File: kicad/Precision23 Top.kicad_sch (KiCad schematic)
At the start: 18 parts, among them J503 Conn_02x03_Odd_Even, J505 Conn_01x06, J506 Conn_01x06, J596 STANDOFF, J597 STANDOFF, J598 STANDOFF, J599 STANDOFF, U501 SAM-M10Q, U502 741G157, U503 741G157, U504 741G157

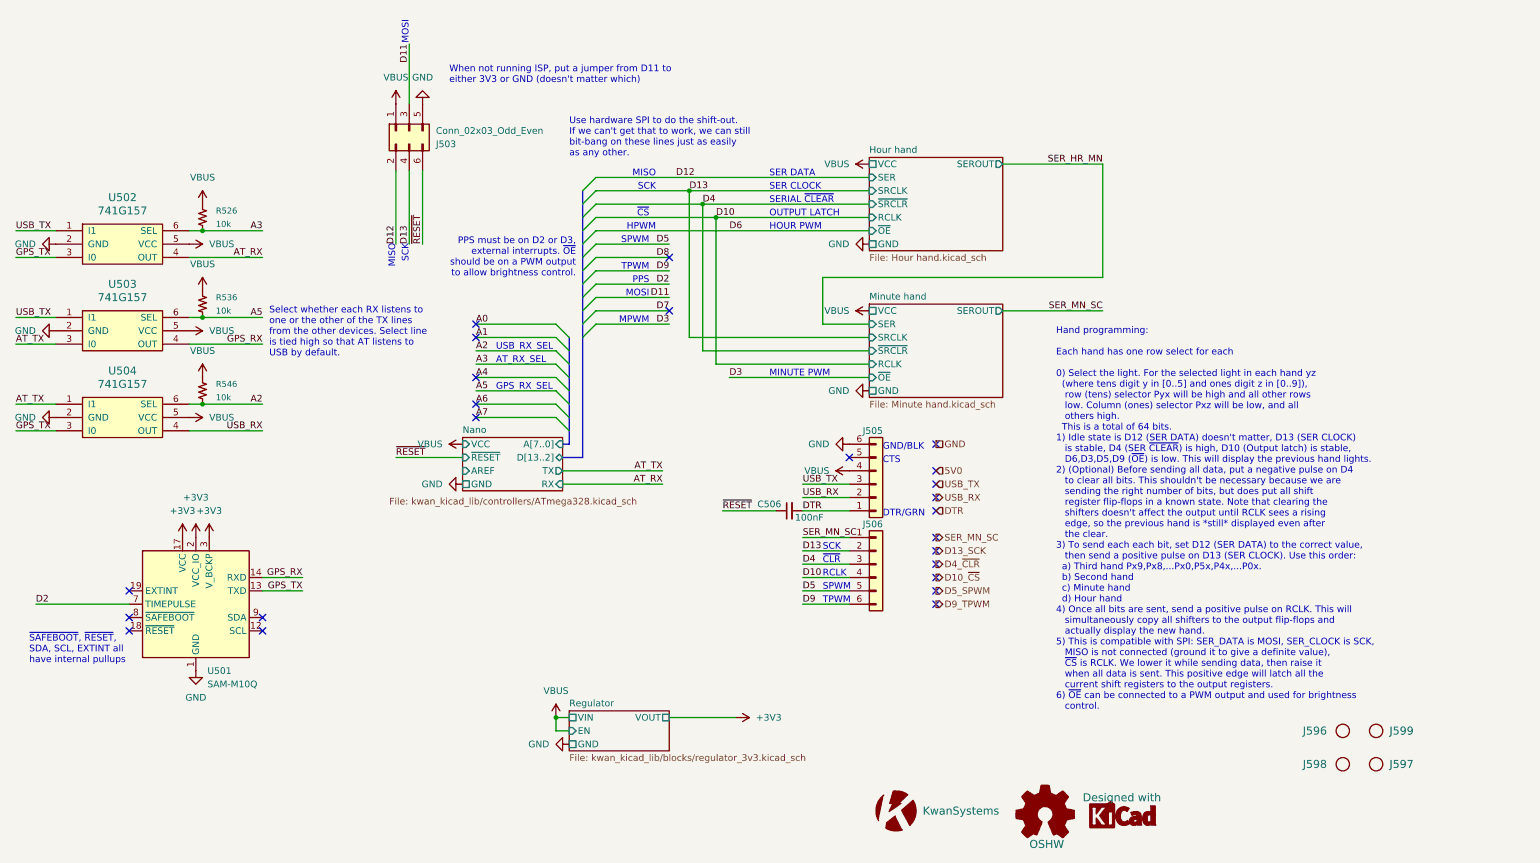
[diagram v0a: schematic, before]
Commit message: Added top and bottom schematics to support refactor of board
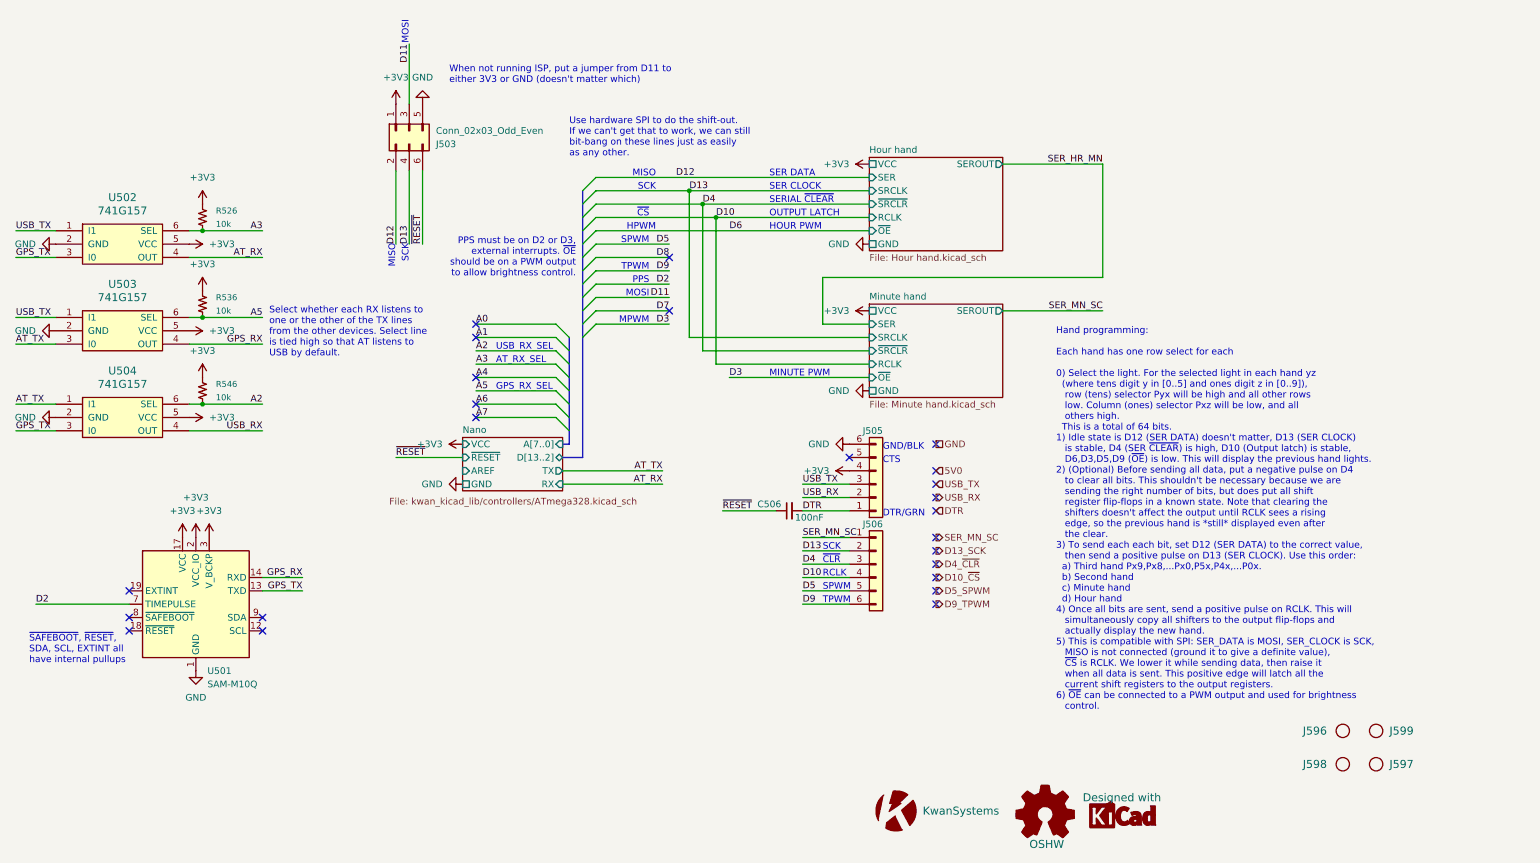
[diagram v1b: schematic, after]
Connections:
- net VBUS is gone; now on net +3V3: J503.1 (Pin_1), J505.4 (Pin_4), R526.1, R536.1, R546.1, U502.5 (VCC), U503.5 (VCC), U504.5 (VCC)
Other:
- removed sheet Regulator

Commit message: Refactored board, put 5V0 on all parts except GPS
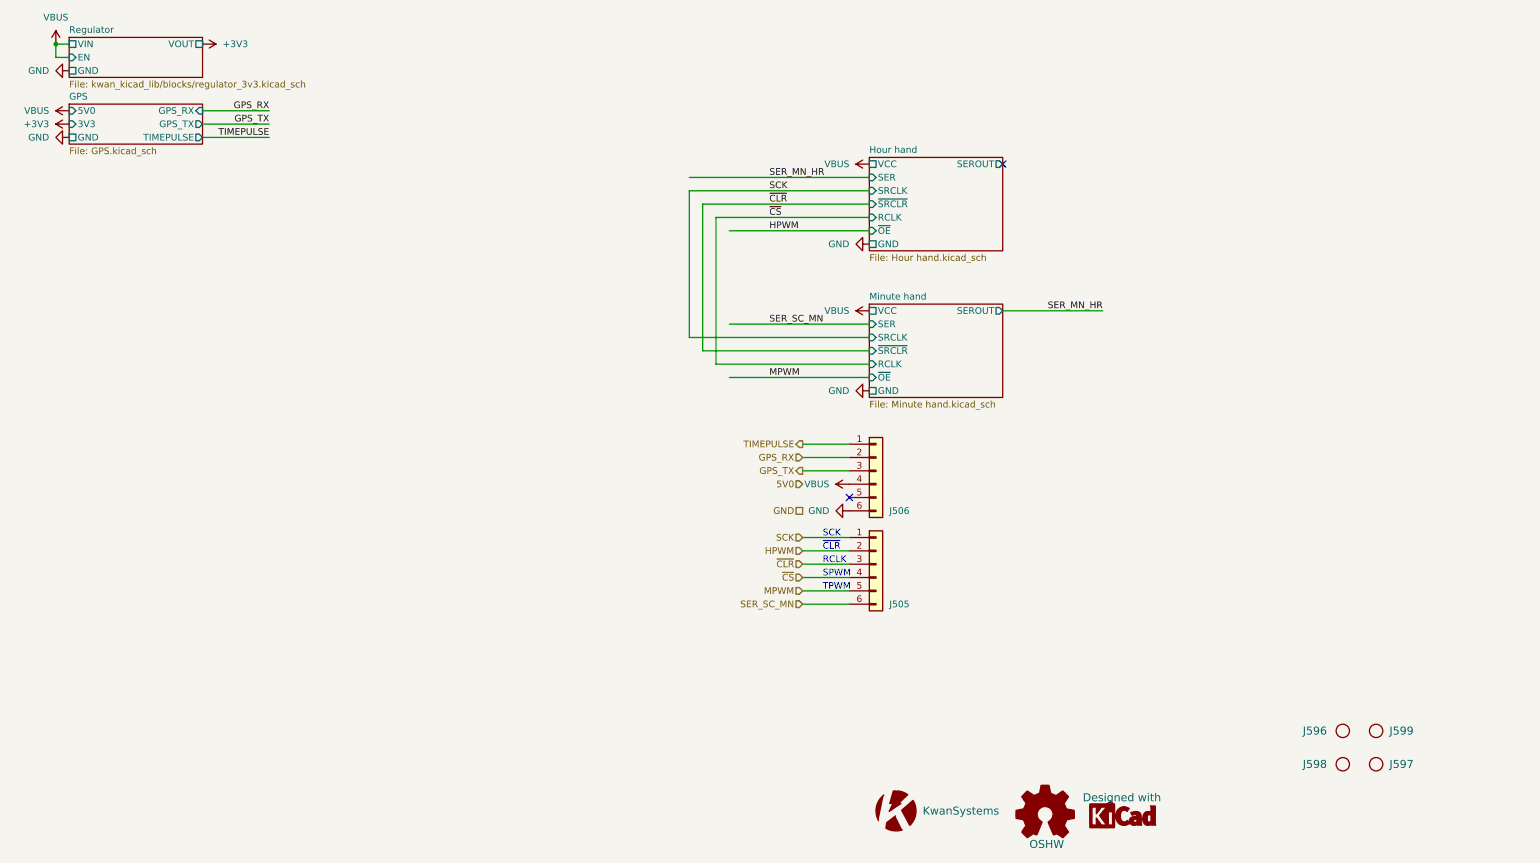
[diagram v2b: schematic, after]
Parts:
- removed C506: 100nF, Capacitor_SMD:C_0603_1608Metric, symbol Device:C_Small
- removed J503: Conn_02x03_Odd_Even, Connector_PinSocket_2.54mm:PinSocket_2x03_P2.54mm_Vertical_SMD, symbol Connector_Generic:Conn_02x03_Odd_Even
- removed R526, R536, R546: 10k, Resistor_SMD:R_0603_1608Metric, symbol KwanSystems:RESISTOR
- removed U501: SAM-M10Q, RF_GPS:ublox_SAM-M8Q, symbol RF_GPS:SAM-M8Q
- removed U502, U503, U504: 741G157, Package_TO_SOT_SMD:SOT-363_SC-70-6, symbol KwanSystems:NC7SZ157
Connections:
- net USB_RX is gone; now on net GPS_RX: J505.2 (Pin_2)
- net USB_TX is gone; now on net GPS_TX: J505.3 (Pin_3)
- net +3V3: no longer J505.4 (Pin_4)
- net D10 renamed ~{CS}
- net D13 renamed HPWM
- net D4 renamed ~{CLR}
- net D5 renamed MPWM
- net D9 renamed SER_SC_MN
- net DTR renamed TIMEPULSE
- net SER_MN_SC renamed SCK
- new net VBUS: J505.4 (Pin_4)
- no-connect marks 24 -> 2
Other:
- removed sheet Nano
- added sheet GPS (GPS.kicad_sch)
- added sheet Regulator (kwan_kicad_lib/blocks/regulator_3v3.kicad_sch)
- note removed: "AT_RX_SEL"
- note removed: "CTS"
- note removed: "DTR/GRN"
- note removed: "GND/BLK"
- note removed: "GPS_RX_SEL"
- note removed: "HOUR PWM"
- note removed: "HPWM"
- note removed: "Hand programming: Each hand has one row select for each 0) Select the light. For the selected light in each hand yz (where tens digit y in [0..5] and ones digit z in [0..9]), row (tens) selector Pyx will be high and all other rows low. Column (ones) selector Pxz will be low, and all others high. This is a total of 64 bits. 1) Idle state is D12 (SER DATA) doesn't matter, D13 (SER CLOCK) is stable,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"
- note removed: "MINUTE PWM"
- note removed: "MISO"
- note removed: "MOSI"
- note removed: "MPWM"
- note removed: "OUTPUT LATCH"
- note removed: "PPS"
- note removed: "PPS must be on D2 or D3, external interrupts. ~{OE} should be on a PWM output to allow brightness control."
- note removed: "SER CLOCK"
- note removed: "SER DATA"
- note removed: "SERIAL ~{CLEAR}"
- note removed: "Select whether each RX listens to one or the other of the TX lines from the other devices. Select line is tied high so that AT listens to USB by default."
- note removed: "USB_RX_SEL"
- note removed: "Use hardware SPI to do the shift-out. If we can't get that to work, we can still bit-bang on these lines just as easily as any other."
- note removed: "When not running ISP, put a jumper from D11 to either 3V3 or GND (doesn't matter which)"
- note removed: "~{CS}"
- note removed: "~{SAFEBOOT}, ~{RESET}, SDA, SCL, EXTINT all have internal pullups"

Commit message: Put MOSFET switch transistors in place. We won't end up using these.
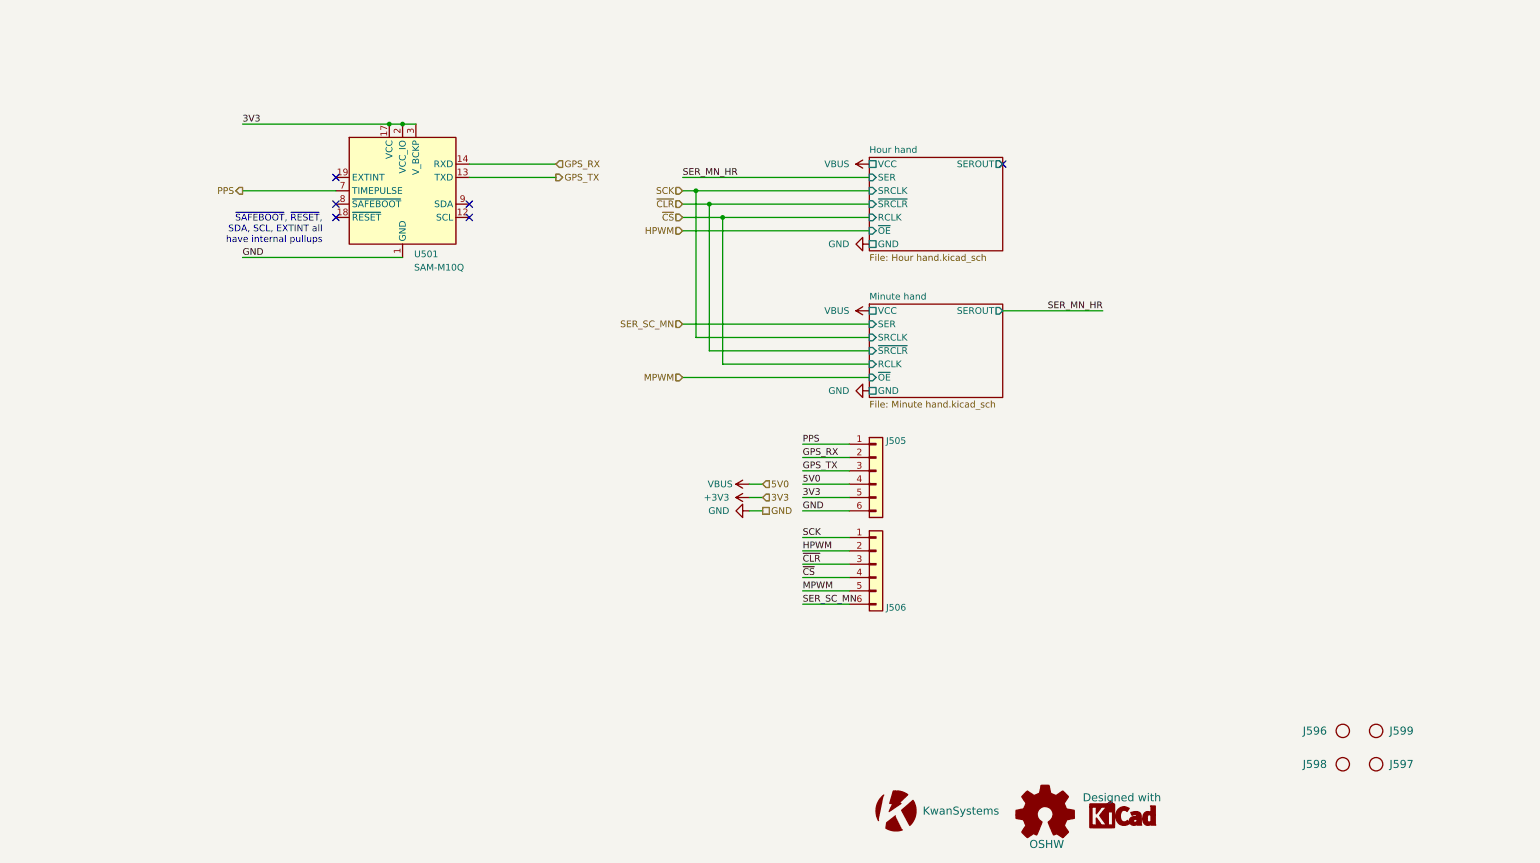
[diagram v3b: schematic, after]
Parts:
- added U501: SAM-M10Q, RF_GPS:ublox_SAM-M8Q, symbol RF_GPS:SAM-M8Q
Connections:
- net +3V3: now also J505.5 (Pin_5), U501.17 (VCC), U501.2 (VCC_IO), U501.3 (V_BCKP)
- net GND: now also U501.1 (GND), U501.10 (GND), U501.11 (GND), U501.15 (GND), U501.16 (GND), U501.20 (GND), U501.4 (GND), U501.5 (GND), U501.6 (GND)
- net GPS_RX: now also U501.14 (RXD)
- net GPS_TX: now also U501.13 (TXD)
- net TIMEPULSE renamed PPS
- net PPS: now also U501.7 (TIMEPULSE)
- no-connect marks 2 -> 6
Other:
- removed sheet GPS
- removed sheet Regulator
- note added: "~{SAFEBOOT}, ~{RESET}, SDA, SCL, EXTINT all have internal pullups"
- note removed: "RCLK"
- note removed: "SCK"
- note removed: "SPWM"
- note removed: "TPWM"
- note removed: "~{CLR}"

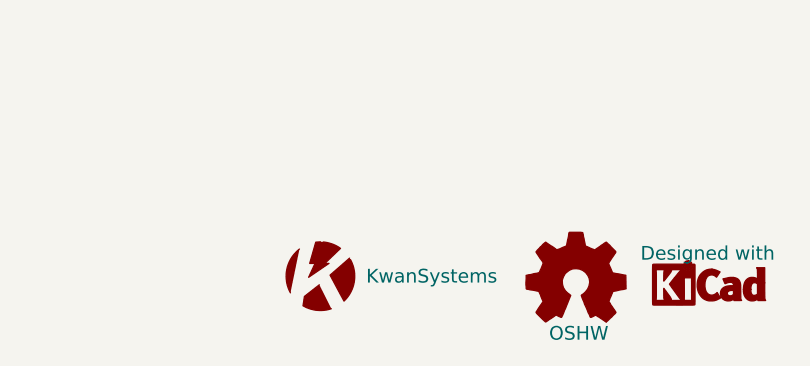
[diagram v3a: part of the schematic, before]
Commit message: Continue wiring MOSFET switches
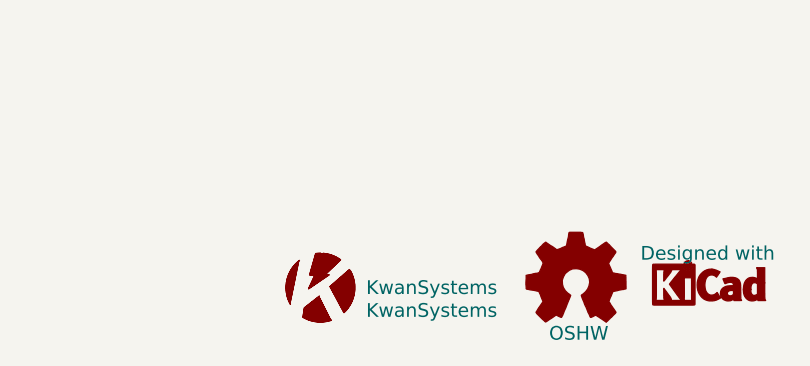
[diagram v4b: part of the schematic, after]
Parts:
- added G102: KwanSystems, KwanSystems:StKwansSoldermask, symbol KwanSystems:KwanSystems
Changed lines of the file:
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@@
     )
   )
-  (symbol (lib_id "KwanSystems:KwanSystems") (at 182.88 171.45 0) (unit 1)
+  (symbol (lib_id "KwanSystems:KwanSystems") (at 182.88 172.72 0) (unit 1)
     (in_bom no) (on_board yes) (dnp no)
-    (property "Reference" "G101" (at 182.88 171.45 0)
+    (property "Reference" "G101" (at 182.88 172.72 0)
       (effects (font (size 1.524 1.524)) hide)
     )
-    (property "Value" "KwanSystems" (at 187.96 171.45 0)
+    (property "Value" "KwanSystems" (at 187.96 172.72 0)
       (effects (font (size 1.524 1.524)) (justify left))
     )
-    (property "Footprint" "KwanSystems:PrecisionKwan" (at 182.88 166.37 0)
+    (property "Footprint" "KwanSystems:PrecisionKwan" (at 182.88 167.64 0)
       (effects (font (size 1.524 1.524)) hide)
     )
-    (property "Datasheet" "" (at 182.88 171.45 0)
+    (property "Datasheet" "" (at 182.88 172.72 0)
       (effects (font (size 1.524 1.524)) hide)
     )
-    (property "Purpose" "Big silkscreen Kwan logo" (at 182.88 171.45 0)
+    (property "Purpose" "Big silkscreen Kwan logo" (at 182.88 172.72 0)
       (effects (font (size 1.27 1.27)) hide)
     )
@@
         )
       )
+    )
+  )
+  (symbol (lib_id "KwanSystems:KwanSystems") (at 182.88 172.72 0) (unit 1)
+    (in_bom no) (on_board yes) (dnp no)
+    (property "Reference" "G102" (at 182.88 172.72 0)
+      (effects (font (size 1.524 1.524)) hide)
+    )
+    (property "Value" "KwanSystems" (at 187.96 175.26 0)
+      (effects (font (size 1.524 1.524)) (justify left))
+    )
+    (property "Footprint" "KwanSystems:StKwansSoldermask" (at 182.88 167.64 0)
+      (effects (font (size 1.524 1.524)) hide)
+    )
+    (property "Datasheet" "" (at 182.88 172.72 0)
+      (effects (font (size 1.524 1.524)) hide)
+    )
+    (property "Purpose" "Small gold Kwan logo" (at 182.88 172.72 0)
+      (effects (font (size 1.27 1.27)) hide)
+    )
+    (instances
+      (project "Precision23"
+        (path "/9151f981-b383-4946-8df4-92ef46ef2206"
+          (reference "G102") (unit 1)
+        )
+        (path "/9151f981-b383-4946-8df4-92ef46ef2206/b9b5a9b9-9a45-4bb4-8a5d-f3809553447a"
+          (reference "G102") (unit 1)
+        )
+        (path "/9151f981-b383-4946-8df4-92ef46ef2206/9f66be35-2744-413f-8b31-a996047a434b"
+          (reference "G103") (unit 1)
+        )
+      )
